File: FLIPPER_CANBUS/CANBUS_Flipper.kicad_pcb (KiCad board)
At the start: 2 copper layers, 67 x 31.3 mm, 17 parts, among them J1 Conn_01x08_Socket, J2 Conn_01x10_Socket, J3 Conn_01x02, U1 MCP2515-xST, U2 MAX3051, Y1 16 Mhz

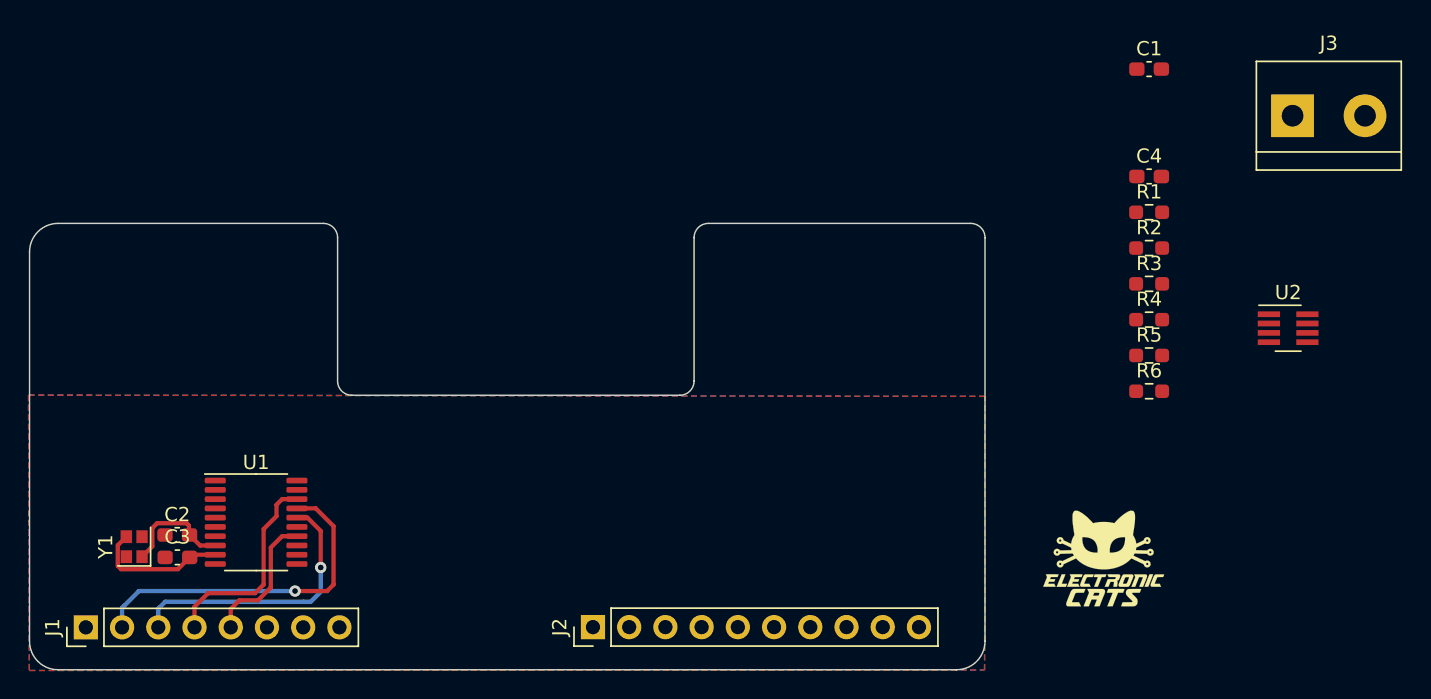
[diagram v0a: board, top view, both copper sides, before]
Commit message: Resistance Correction
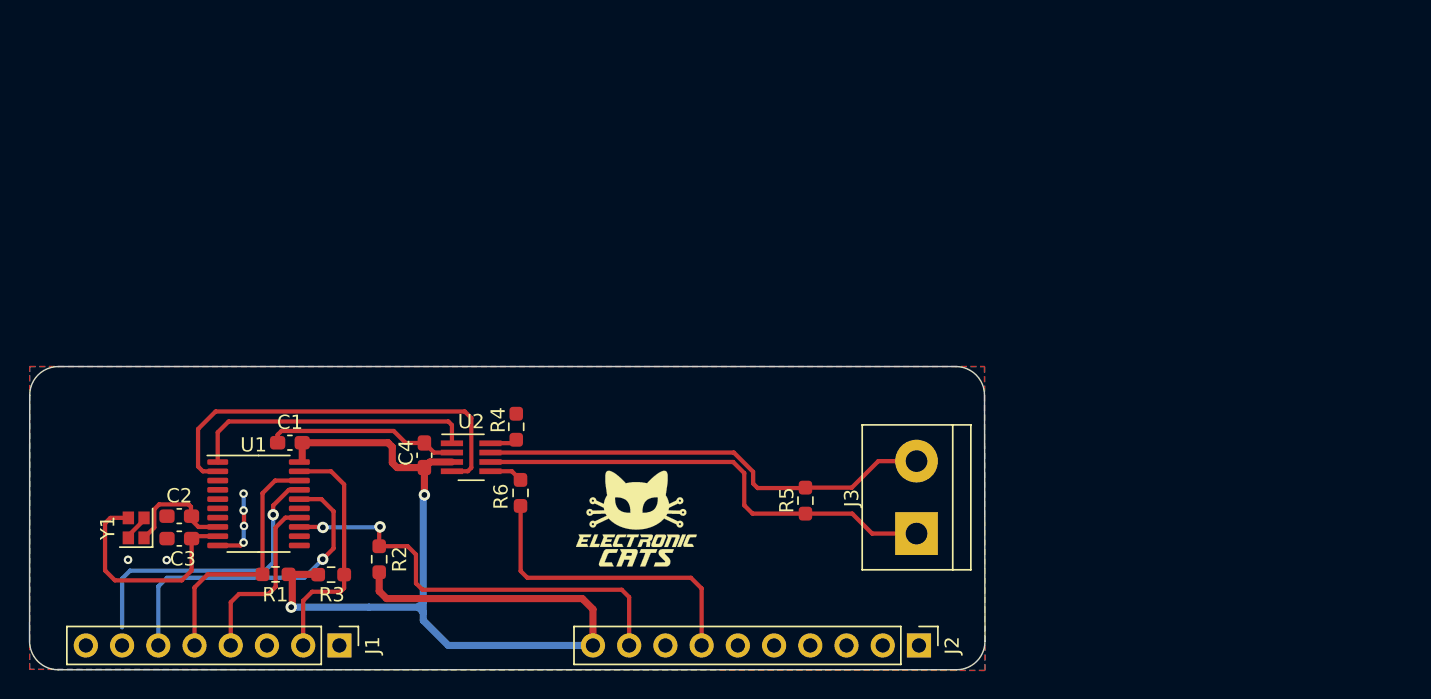
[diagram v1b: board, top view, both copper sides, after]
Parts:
- moved R1 66.3 mm to (126.3, 104.0)
- moved C1 65.7 mm to (127.3, 94.8)
- moved R3 60.9 mm to (130.2, 104.0)
- moved R2 58.2 mm to (133.6, 102.9), turned to -90 degrees
- moved U2 58.0 mm to (140.1, 95.8)
- moved C4 54.5 mm to (136.8, 95.6), turned to -90 degrees
- moved R4 45.0 mm to (143.2, 93.6), turned to 90 degrees
- moved R6 44.7 mm to (143.5, 98.3), turned to 90 degrees
- moved J3 39.4 mm to (171.3, 101.1), turned to 90 degrees
- moved G*** 32.9 mm to (151.6, 100.1)
- moved R5 26.2 mm to (163.5, 98.8), turned to -90 degrees
- moved J2 22.9 mm to (171.4, 109.0), turned to -90 degrees
- moved J1 17.8 mm to (130.8, 109.0), turned to -90 degrees
- moved Y1 1.33 mm to (116.6, 100.7)
- moved C2 1.33 mm to (119.6, 99.9)
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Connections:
- J1 pad 1: +5V -> GND
- J1 pad 2: /SDO -> /RST
- J1 pad 3: /SDI -> unconnected-(J1-Pin_3-Pad3)
- J1 pad 4: /CS -> /SCK
- J1 pad 5: /SCK -> /CS
- J1 pad 6: unconnected-(J1-Pin_6-Pad6) -> /SDI
- J1 pad 7: /RST -> /SDO
- J1 pad 8: GND -> +5V
- J2 pad 1: +3.3V -> GND
- J2 pad 10: GND -> +3.3V
- J2 pad 2: /INT -> unconnected-(J2-Pin_2-Pad2)
- J2 pad 3: GND -> unconnected-(J2-Pin_3-Pad3)
- J2 pad 4: /SHDN -> unconnected-(J2-Pin_4-Pad4)
- J2 pad 7: unconnected-(J2-Pin_7-Pad7) -> /SHDN
- J2 pad 8: unconnected-(J2-Pin_8-Pad8) -> GND
- J2 pad 9: unconnected-(J2-Pin_9-Pad9) -> /INT
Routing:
- net +3.3V: track 0.00 -> 70.4 mm, vias 0 -> 2
- net /CANL: track 0.00 -> 33.3 mm
- net /CANH: track 0.00 -> 32.2 mm
- net /INT: track 0.00 -> 30.7 mm, vias 0 -> 2
- net /RXD: track 0.00 -> 28.9 mm
- net /SHDN: track 0.00 -> 21.8 mm
- net GND: track 0.00 -> 20.7 mm, vias 0 -> 6
- net /TXD: track 0.00 -> 20.2 mm
- net /RST: track 0.00 -> 17.2 mm
- net Net-(U1-OSC1): track 9.65 -> 16.1 mm
- net /SDI: track 19.5 -> 22.9 mm
- net /CS: track 14.5 -> 17.9 mm
- net /SDO: track 24.1 -> 20.8 mm
- net /SCK: track 9.68 -> 12.7 mm
- net Net-(U2-SHDN): track 0.00 -> 2.36 mm
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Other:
- board size 67 x 31.3 mm -> 67 x 21.3 mm

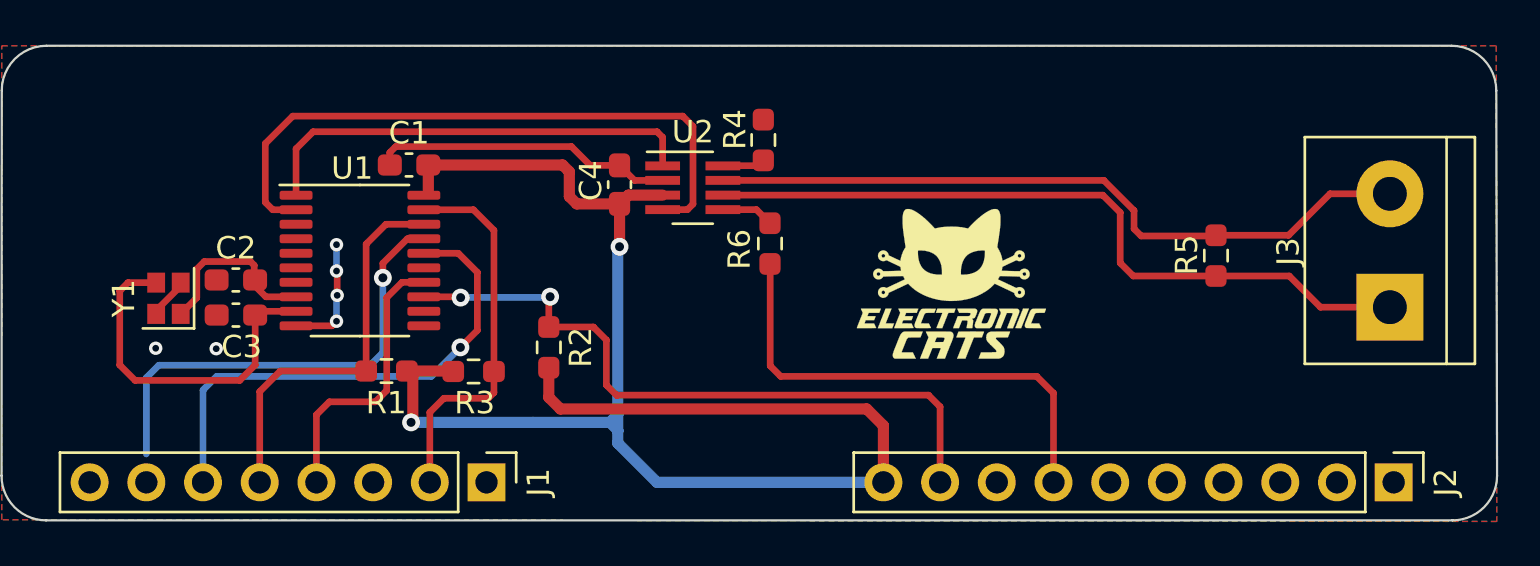
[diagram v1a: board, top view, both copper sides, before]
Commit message: Add labels CANBUS
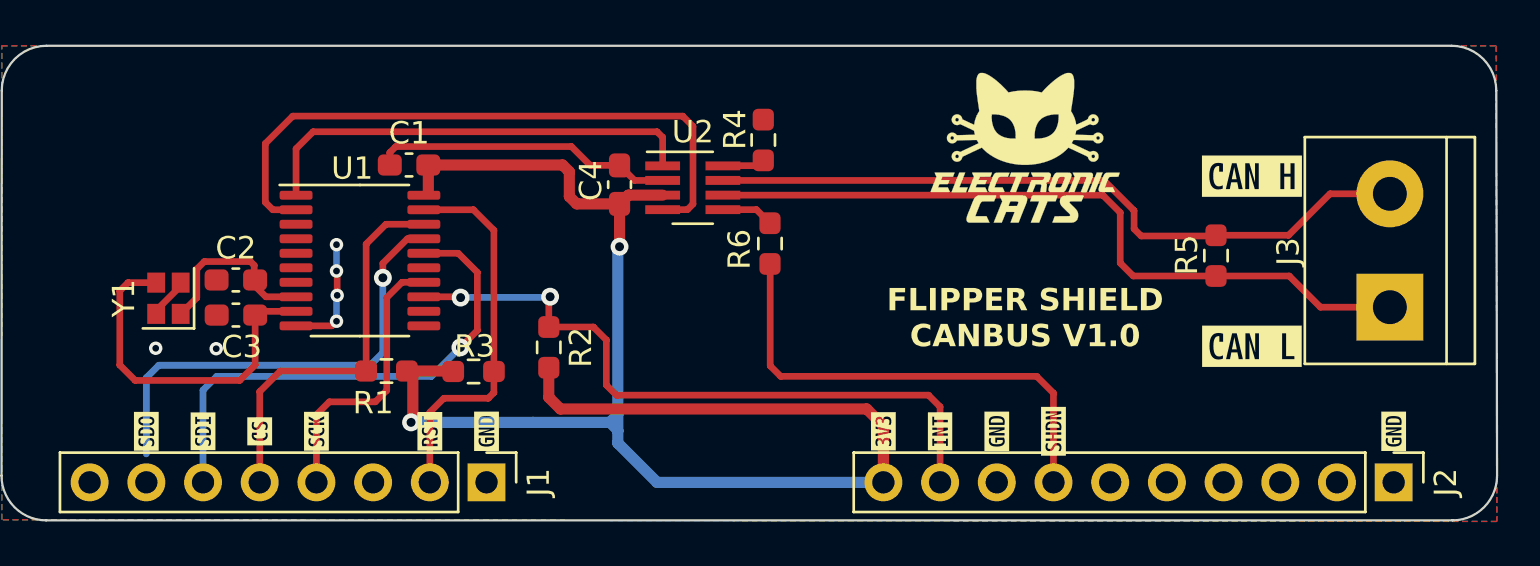
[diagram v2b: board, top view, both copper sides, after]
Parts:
- added G***: LOGO, Aesthetics:electronic_cats_logo_8x6, F.Cu at (154.9, 94.0)
- added REF**: OSHW-Logo2_14.6x12mm_SilkScreen, Symbol:OSHW-Logo2_14.6x12mm_SilkScreen, B.Cu at (121.9, 99.1)
- added kibuzzard-65B92F42: G***, kibuzzard-65B92F42, F.Cu at (130.8, 106.7)
- added kibuzzard-65B92F42: G***, kibuzzard-65B92F42, F.Cu at (171.4, 106.7)
- added kibuzzard-65B92F42: G***, kibuzzard-65B92F42, F.Cu at (153.7, 106.7)
- added kibuzzard-65B92F61: G***, kibuzzard-65B92F61, F.Cu at (156.2, 106.7)
- added kibuzzard-65B92F6C: G***, kibuzzard-65B92F6C, F.Cu at (151.1, 106.7)
- added kibuzzard-65B92F78: G***, kibuzzard-65B92F78, F.Cu at (148.6, 106.7)
- added kibuzzard-65B92F83: G***, kibuzzard-65B92F83, F.Cu at (128.3, 106.7)
- added kibuzzard-65B92F91: G***, kibuzzard-65B92F91, F.Cu at (123.2, 106.7)
- added kibuzzard-65B92F9D: G***, kibuzzard-65B92F9D, F.Cu at (118.1, 106.7)
- added kibuzzard-65B92FB1: G***, kibuzzard-65B92FB1, F.Cu at (115.6, 106.7)
- added kibuzzard-65B92FBC: G***, kibuzzard-65B92FBC, F.Cu at (120.7, 106.7)
- added kibuzzard-65B92FFC: G***, kibuzzard-65B92FFC, F.Cu at (165.1, 95.2)
- added kibuzzard-65B9300E: G***, kibuzzard-65B9300E, F.Cu at (165.1, 102.9)
- G***: moved to B.Cu
- moved G*** 6.93 mm to (154.9, 94.0), turned to 180 degrees
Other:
- board text added: "FLIPPER SHIELD CANBUS V1.0"

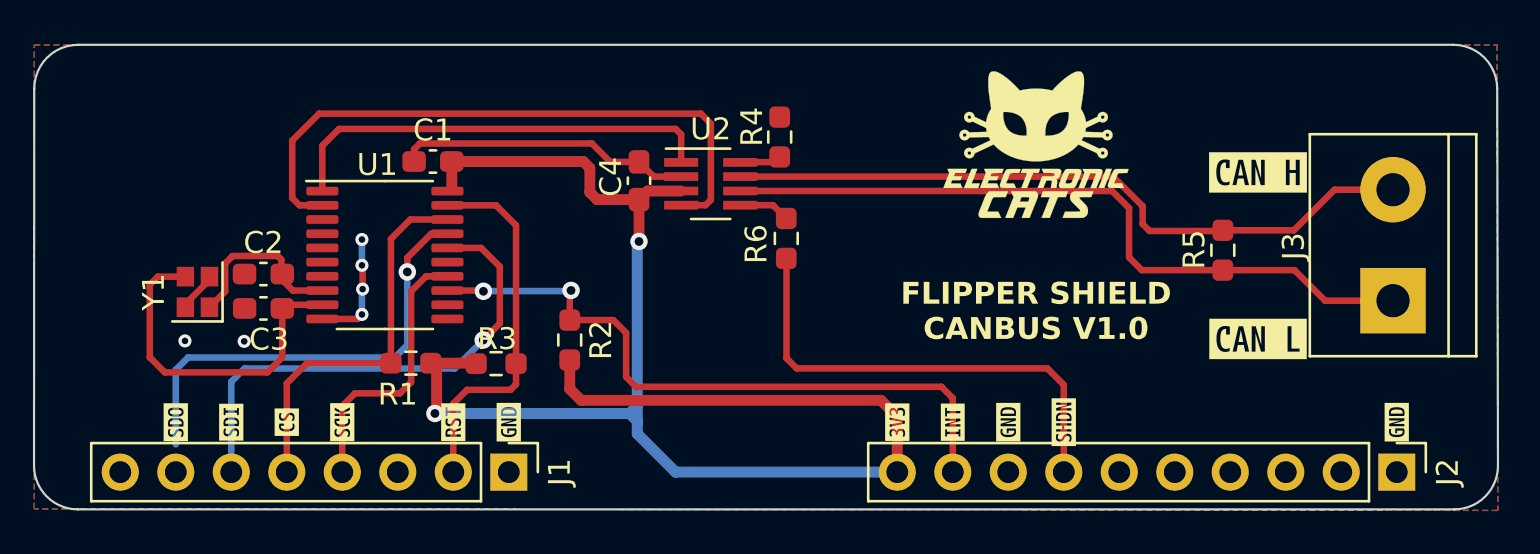
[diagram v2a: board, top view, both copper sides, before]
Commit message: feat(Hw):Update_pins_SDO_SDI
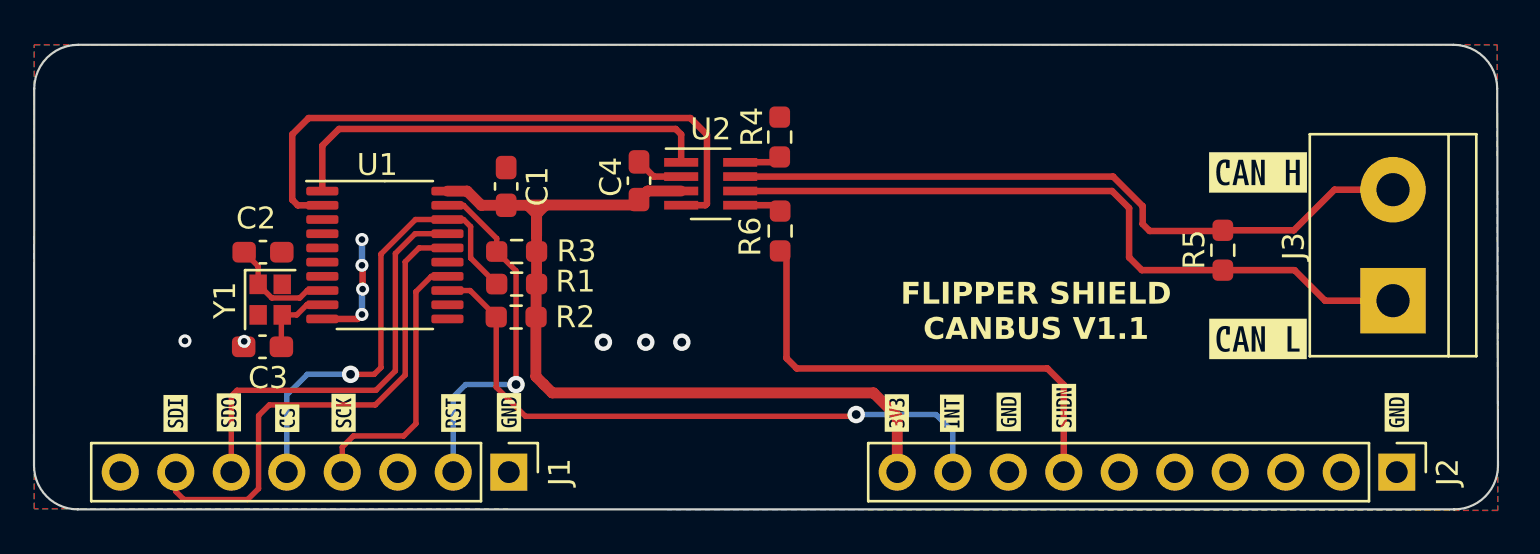
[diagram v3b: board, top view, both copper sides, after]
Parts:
- removed G*** (x2): LOGO, Aesthetics:electronic_cats_logo_8x6
- removed REF**: OSHW-Logo2_14.6x12mm_SilkScreen, Symbol:OSHW-Logo2_14.6x12mm_SilkScreen
- moved R1 6.04 mm to (131.2, 100.4)
- moved R3 5.22 mm to (131.2, 98.9), turned to 180 degrees
- moved C1 3.54 mm to (130.7, 95.9), turned to -90 degrees
- moved Y1 3.35 mm to (119.9, 101.1), turned to -90 degrees
- moved R2 2.67 mm to (131.1, 101.9), turned to 0 degrees
- moved kibuzzard-65B92F9D 2.58 mm to (115.6, 106.3)
- moved kibuzzard-65B92FB1 2.47 mm to (118.0, 106.2)
- moved C3 1.76 mm to (119.5, 103.2)
- moved C2 1.00 mm to (119.6, 98.9), turned to 180 degrees
- moved kibuzzard-65B92F61 0.66 mm to (156.2, 106.0)
- moved kibuzzard-65B92F42 0.47 mm to (153.7, 106.2)
- moved kibuzzard-65B92F42 0.45 mm to (130.8, 106.2)
- moved kibuzzard-65B92F42 0.45 mm to (171.4, 106.2)
- moved R6 0.44 mm to (143.2, 97.9)
- moved kibuzzard-65B92F91 0.43 mm to (123.2, 106.2)
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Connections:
- J1 pad 6: /SDI -> /SDO
- J1 pad 7: /SDO -> /SDI
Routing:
- net +3.3V: track 70.4 -> 40.7 mm, vias 2 -> 0
- net GND: track 20.7 -> 7.56 mm, vias 6 -> 9
- net Net-(U1-OSC1): track 16.1 -> 3.51 mm
- net /CS: track 17.9 -> 21.6 mm, vias 0 -> 1
- net Net-(U1-OSC2): track 7.93 -> 5.07 mm
- net /SDO: track 20.8 -> 19.6 mm, vias 1 -> 0
- net /INT: track 30.7 -> 29.6 mm, vias 2 -> 1
- net /RST: track 17.2 -> 16.5 mm, vias 0 -> 1
- net /RXD: track 28.9 -> 28.4 mm
- net /SDI: track 22.9 -> 23.2 mm, vias 1 -> 0
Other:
- board text added: "FLIPPER SHIELD CANBUS V1.1"

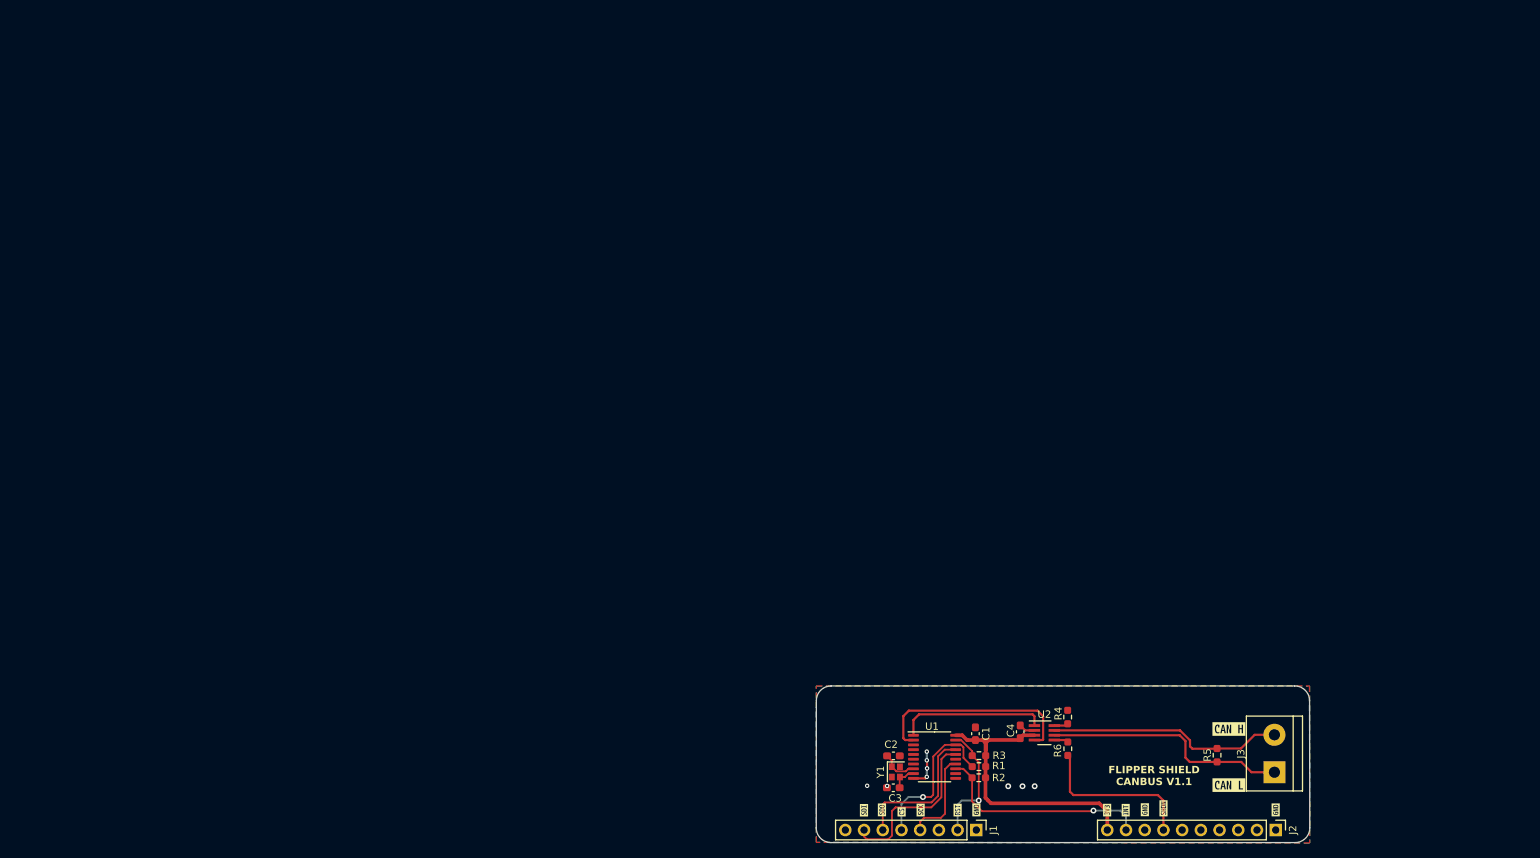
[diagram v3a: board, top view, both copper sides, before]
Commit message: feat(hw):Canbus Shield jumper added
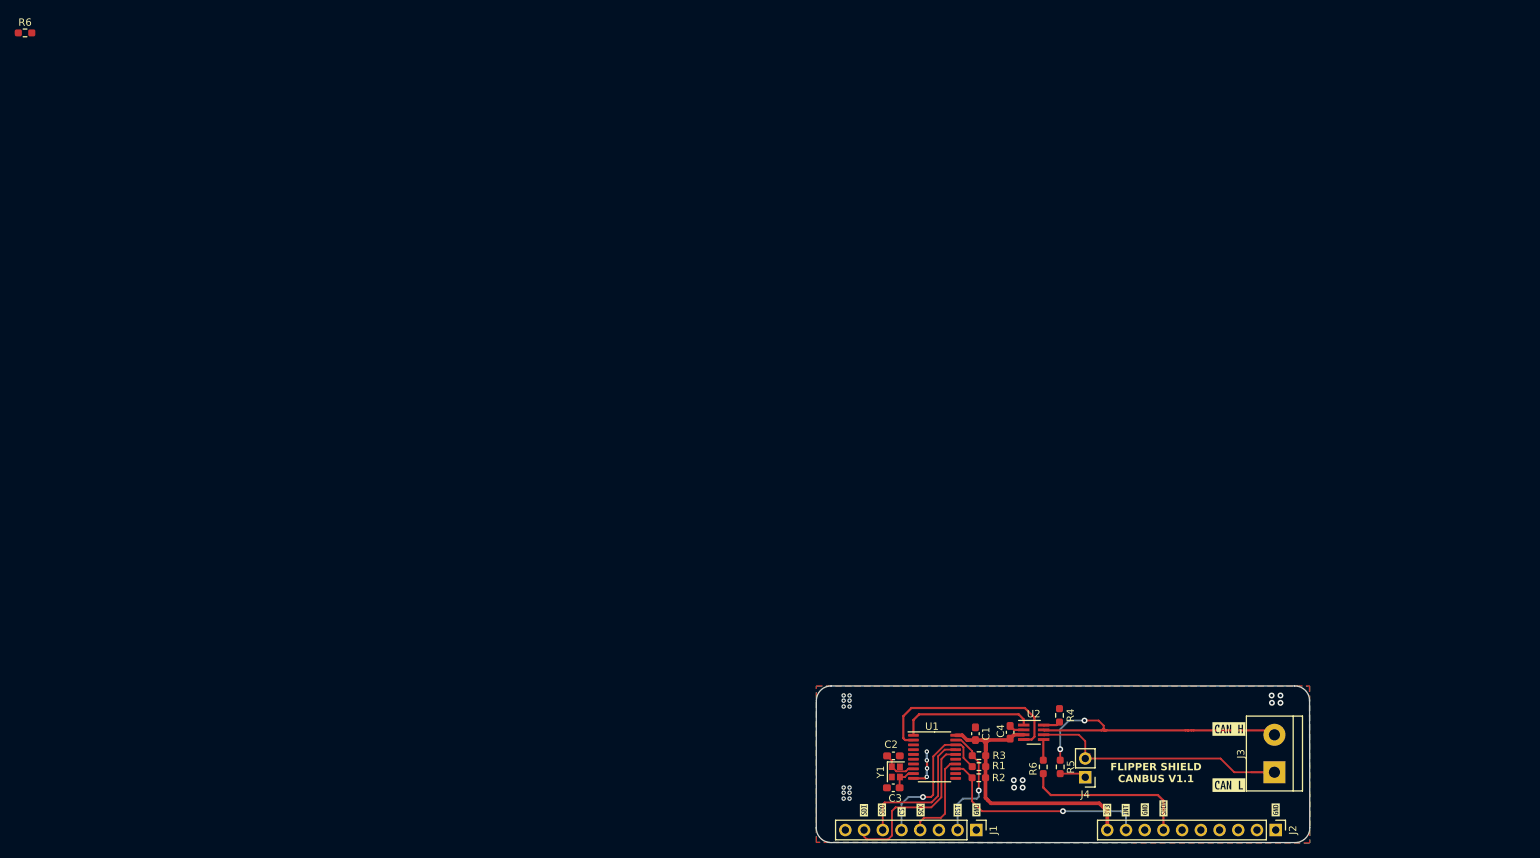
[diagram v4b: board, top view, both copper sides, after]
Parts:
- added J4: Conn_01x02_Socket, Connector_PinHeader_2.54mm:PinHeader_1x02_P2.54mm_Vertical, F.Cu at (145.6, 101.8)
- added R6: 0, Resistor_SMD:R_0603_1608Metric_Pad0.98x0.95mm_HandSolder, F.Cu at (1.68, 0.76)
- moved R5 21.3 mm to (142.2, 100.4)
- moved R6 4.15 mm to (139.9, 100.4)
- moved U2 1.45 mm to (138.6, 95.7)
- moved C4 1.37 mm to (135.4, 95.7)
- moved R4 1.13 mm to (142.1, 93.4)
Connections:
- R5 pad 2: /CANL -> Net-(J4-Pin_1)
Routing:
- net /CANH: track 32.2 -> 43.8 mm, vias 0 -> 2
- net Net-(J4-Pin_1): track 0.00 -> 3.60 mm
- net /CANL: track 33.3 -> 35.8 mm
- net /TXD: track 20.2 -> 18.4 mm
- net +3.3V: track 40.7 -> 39.3 mm
- net /RXD: track 28.4 -> 27.5 mm
- net Net-(U2-SHDN): track 1.94 -> 2.83 mm
- net /SHDN: track 22.2 -> 22.9 mm
- net Net-(U2-RS): track 1.82 -> 2.40 mm
- net GND: track 7.56 -> 7.42 mm, vias 9 -> 24
